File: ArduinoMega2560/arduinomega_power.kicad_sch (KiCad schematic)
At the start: 19 parts, among them IC5 LM358D, T2 FDN340P, U3 LP2986AILD-3.3/NOPB

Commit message: Annotation problem
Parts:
- renumbered RN5C1 to RN5C, IC5 to U3, U3 to UP3
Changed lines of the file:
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@@
   (symbol (lib_id "PCM_Amplifier_Operational_AKL:LM358D") (at 101.6 104.14 0) (unit 1)
     (in_bom yes) (on_board yes) (dnp no)
-    (property "Reference" "IC5" (at 113.03 99.9491 0)
+    (property "Reference" "U3" (at 113.03 99.9491 0)
       (effects (font (size 1.27 1.27)))
     )
@@
       (project "ArduinoMega2560"
         (path "/9c604cc5-1a6f-41a9-b015-ecf51c009c14/7c89fbb2-6a37-4d58-a5e8-241333b4d617"
-          (reference "IC5") (unit 1)
+          (reference "U3") (unit 1)
         )
       )
@@
   (symbol (lib_id "PCM_Amplifier_Operational_AKL:LM358D") (at 57.15 127 0) (unit 2)
     (in_bom yes) (on_board yes) (dnp no)
-    (property "Reference" "IC5" (at 58.42 116.84 0)
+    (property "Reference" "U3" (at 58.42 116.84 0)
       (effects (font (size 1.27 1.27)))
     )
@@
       (project "ArduinoMega2560"
         (path "/9c604cc5-1a6f-41a9-b015-ecf51c009c14/7c89fbb2-6a37-4d58-a5e8-241333b4d617"
-          (reference "IC5") (unit 2)
+          (reference "U3") (unit 2)
         )
       )
@@
   (symbol (lib_id "TI_LP2986AILD-3.3-NOPB:LP2986AILD-3.3_NOPB") (at 97.79 144.78 0) (unit 1)
     (in_bom yes) (on_board yes) (dnp no) (fields_autoplaced)
-    (property "Reference" "U3" (at 120.65 134.62 0)
+    (property "Reference" "UP3" (at 120.65 134.62 0)
       (effects (font (size 1.524 1.524)))
     )
@@
       (project "ArduinoMega2560"
         (path "/9c604cc5-1a6f-41a9-b015-ecf51c009c14/7c89fbb2-6a37-4d58-a5e8-241333b4d617"
-          (reference "U3") (unit 1)
+          (reference "UP3") (unit 1)
         )
       )
@@
       (effects (font (size 1.27 1.27)) hide)
     )
-    (property "Value" "GND1" (at 152.4 166.37 0)
-      (effects (font (size 1.27 1.27)))
+    (property "Value" "GND1" (at 154.94 162.56 0)
+      (effects (font (size 1.27 1.27)) (justify left))
     )
     (property "Footprint" "" (at 152.4 161.29 0)
@@
   (symbol (lib_id "PCM_Resistor_AKL:R_0603") (at 26.67 128.27 180) (unit 1)
     (in_bom yes) (on_board yes) (dnp no)
-    (property "Reference" "RN5C1" (at 29.21 127 0)
+    (property "Reference" "RN5C" (at 29.21 127 0)
       (effects (font (size 1.27 1.27)) (justify right))
     )
@@
       (project "ArduinoMega2560"
         (path "/9c604cc5-1a6f-41a9-b015-ecf51c009c14/7c89fbb2-6a37-4d58-a5e8-241333b4d617"
-          (reference "RN5C1") (unit 1)
-        )
-      )
+          (reference "RN5C") (unit 1)
+        )
+      )

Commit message: Daily update
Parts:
- renumbered RN5C to RN5C1

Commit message: Update label
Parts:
- renumbered LED_L1 to LED_PB7, LED_ON1 to ON1, RN3C1 to RN33, RN3D1 to RN34, RN5B1 to RN52, RN5C1 to RN53
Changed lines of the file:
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@@
 		(on_board yes)
 		(dnp no)
-		(property "Reference" "LED_ON1"
+		(property "Reference" "ON1"
 			(at 147.0025 95.25 0)
 			(effects
@@
 			(project "ArduinoMega2560"
 				(path "/9c604cc5-1a6f-41a9-b015-ecf51c009c14/7c89fbb2-6a37-4d58-a5e8-241333b4d617"
-					(reference "LED_ON1")
+					(reference "ON1")
 					(unit 1)
 				)
@@
 		(on_board yes)
 		(dnp no)
-		(property "Reference" "RN3C1"
+		(property "Reference" "RN33"
 			(at 158.75 96.52 90)
 			(effects
@@
 			(project "ArduinoMega2560"
 				(path "/9c604cc5-1a6f-41a9-b015-ecf51c009c14/7c89fbb2-6a37-4d58-a5e8-241333b4d617"
-					(reference "RN3C1")
+					(reference "RN33")
 					(unit 1)
 				)
@@
 		(on_board yes)
 		(dnp no)
-		(property "Reference" "RN5B1"
+		(property "Reference" "RN52"
 			(at 29.21 144.78 0)
 			(effects
@@
 			(project "ArduinoMega2560"
 				(path "/9c604cc5-1a6f-41a9-b015-ecf51c009c14/7c89fbb2-6a37-4d58-a5e8-241333b4d617"
-					(reference "RN5B1")
+					(reference "RN52")
 					(unit 1)
 				)
@@
 		(on_board yes)
 		(dnp no)
-		(property "Reference" "RN3D1"
+		(property "Reference" "RN34"
 			(at 158.75 109.22 90)
 			(effects
@@
 			(project "ArduinoMega2560"
 				(path "/9c604cc5-1a6f-41a9-b015-ecf51c009c14/7c89fbb2-6a37-4d58-a5e8-241333b4d617"
-					(reference "RN3D1")
+					(reference "RN34")
 					(unit 1)
 				)
@@
 		(on_board yes)
 		(dnp no)
-		(property "Reference" "RN5C1"
+		(property "Reference" "RN53"
 			(at 29.21 127 0)
 			(effects
@@
 			(project "ArduinoMega2560"
 				(path "/9c604cc5-1a6f-41a9-b015-ecf51c009c14/7c89fbb2-6a37-4d58-a5e8-241333b4d617"
-					(reference "RN5C1")
+					(reference "RN53")
 					(unit 1)
 				)
@@
 		(dnp no)
 		(fields_autoplaced yes)
-		(property "Reference" "LED_L1"
+		(property "Reference" "LED_PB7"
 			(at 147.0025 107.95 0)
 			(effects
@@
 			(project "ArduinoMega2560"
 				(path "/9c604cc5-1a6f-41a9-b015-ecf51c009c14/7c89fbb2-6a37-4d58-a5e8-241333b4d617"
-					(reference "LED_L1")
-					(unit 1)
-				)
+					(reference "LED_PB7")
+					(unit 1)
+				)

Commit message: Tracing
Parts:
- removed UP2: MC33269DTRK-5.0G, DPAK-3_ONS, symbol ON_Semi-MC33269DTRK-5.0G:MC33269DTRK-5.0G
- added U4: MC33269DTRK-5.0G, LDO_MC33269DTRK-5.0G_Onsemi:DPAK-3_ONS, symbol LDO_MC33269DTRK-5.0G_Onsemi:MC33269DTRK-5.0G
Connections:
- net GND1 is gone; now on net GND: C13.2
- net GNDPWR is gone; now on net GND: C2.2, Cp1.2, Jack1.2, Jack1.3
- net +5V: now also U4.2 (VOUT)
- net GND: now also U4.1 (GND/ADJ)
- net VCC renamed VIN
- net VIN: now also U4.3 (VIN)

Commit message: Update Trace
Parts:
- UP2: renamed from U4; footprint LDO_MC33269DTRK-5.0G_Onsemi:DPAK-3_ONS -> LDO_MC33269DTRK_5_0G_Onsemi:DPAK-3_ONS
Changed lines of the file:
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@@
 		(dnp no)
 		(fields_autoplaced yes)
-		(property "Reference" "U4"
+		(property "Reference" "UP2"
 			(at 99.06 62.23 0)
 			(effects
@@
 			)
 		)
-		(property "Footprint" "LDO_MC33269DTRK-5.0G_Onsemi:DPAK-3_ONS"
+		(property "Footprint" "LDO_MC33269DTRK_5_0G_Onsemi:DPAK-3_ONS"
 			(at 89.916 83.566 0)
 			(effects
@@
 			(project ""
 				(path "/9c604cc5-1a6f-41a9-b015-ecf51c009c14/7c89fbb2-6a37-4d58-a5e8-241333b4d617"
-					(reference "U4")
+					(reference "UP2")
 					(unit 1)
 				)

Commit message: Update
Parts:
- added J3, J4: PINHD_1x2_Male, Connector_PinHeader_2.54mm:PinHeader_1x02_P2.54mm_Vertical, symbol PCM_SL_Pin_Headers:PINHD_1x2_Male
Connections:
- net +5V: now also J3.1, J3.2
- net GND: now also J4.1, J4.2

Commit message: Update
Using Rev3
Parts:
- removed C11: 100nF_0603_16V, PCM_4ms_Capacitor:C_0603, symbol PCM_4ms_Capacitor:100nF_0603_16V
- removed J3, J4: PINHD_1x2_Male, Connector_PinHeader_2.54mm:PinHeader_1x02_P2.54mm_Vertical, symbol PCM_SL_Pin_Headers:PINHD_1x2_Male
- removed T2: FDN340P, PCM_Package_TO_SOT_SMD_AKL:SuperSOT-3, symbol PCM_Transistor_MOSFET_AKL:FDN340P
- removed U3: LM358D, PCM_Package_SO_AKL:SO-8_3.9x4.9mm_P1.27mm, symbol PCM_Amplifier_Operational_AKL:LM358D
- removed UP1: MC33269ST-5T3G, ON_Semi-MC33269ST-3.3T3G:ON_Semi-CASE_318E04_ISSUE_N-0-0-0, symbol ON_Semi-MC33269ST-3.3T3G:MC33269ST-3.3T3G
- removed UP2: MC33269DTRK-5.0G, LDO_MC33269DTRK_5_0G_Onsemi:DPAK-3_ONS, symbol LDO_MC33269DTRK-5.0G_Onsemi:MC33269DTRK-5.0G
- removed UP3: LP2986AILD-3.3/NOPB, TI_LP2986AILD-3.3-NOPB:LDC08A, symbol TI_LP2986AILD-3.3-NOPB:LP2986AILD-3.3_NOPB
- added PS1: LD1117S50CTR, LDO_LD1117S50CTR_STMicroelectronics:SOT-223_STM, symbol LDO_LD1117S50CTR_STMicroelectronics:LD1117S50CTR
- added PS2: LP2985-3.3, Package_TO_SOT_SMD:SOT-23-5, symbol Regulator_Linear:LP2985-3.3
- added T1: PMV48XP_215, TO-236_SOT23_NEX, symbol MOSFET_PMV48XP,215_Nexperia:PMV48XP_215
- added U3: LMV358IDGK, PCM_Package_SO_AKL:MSOP-8_3x3mm_P0.65mm, symbol PCM_Amplifier_Operational_AKL:LMV358IDGK
- C13: Display 0.1uF -> 1uF
- renumbered RN33 to RN31, RN34 to RN32, RN52 to RN54
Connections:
- net +3.3V: now also PS2.5 (VOUT), U3.6 (-)
- net +5V: now also PS1.2 (VOUT), PS2.1 (VIN), PS2.3 (ON/~{OFF}), T1.2 (S), U3.8 (V+)
- net GATE_CMD: now also T1.1 (G), U3.7
- net GND: now also PS1.1 (ADJ/GND), PS2.2 (GND), U3.4 (V-)
- net PB7: now also U3.3 (+); no longer RN32.2
- net USBVCC: now also T1.3 (D)
- net VIN: now also PS1.3 (VIN)
- net CMP: now reaches C12.1, RN53.1, RN54.2
- net CMP: now also U3.5 (+)
- new net: RN32.2, U3.1, U3.2 (-)
- no-connect marks 6 -> 1
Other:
- moved on the sheet: C13, Cp2, LED_PB7, ON1, RN31, RN32

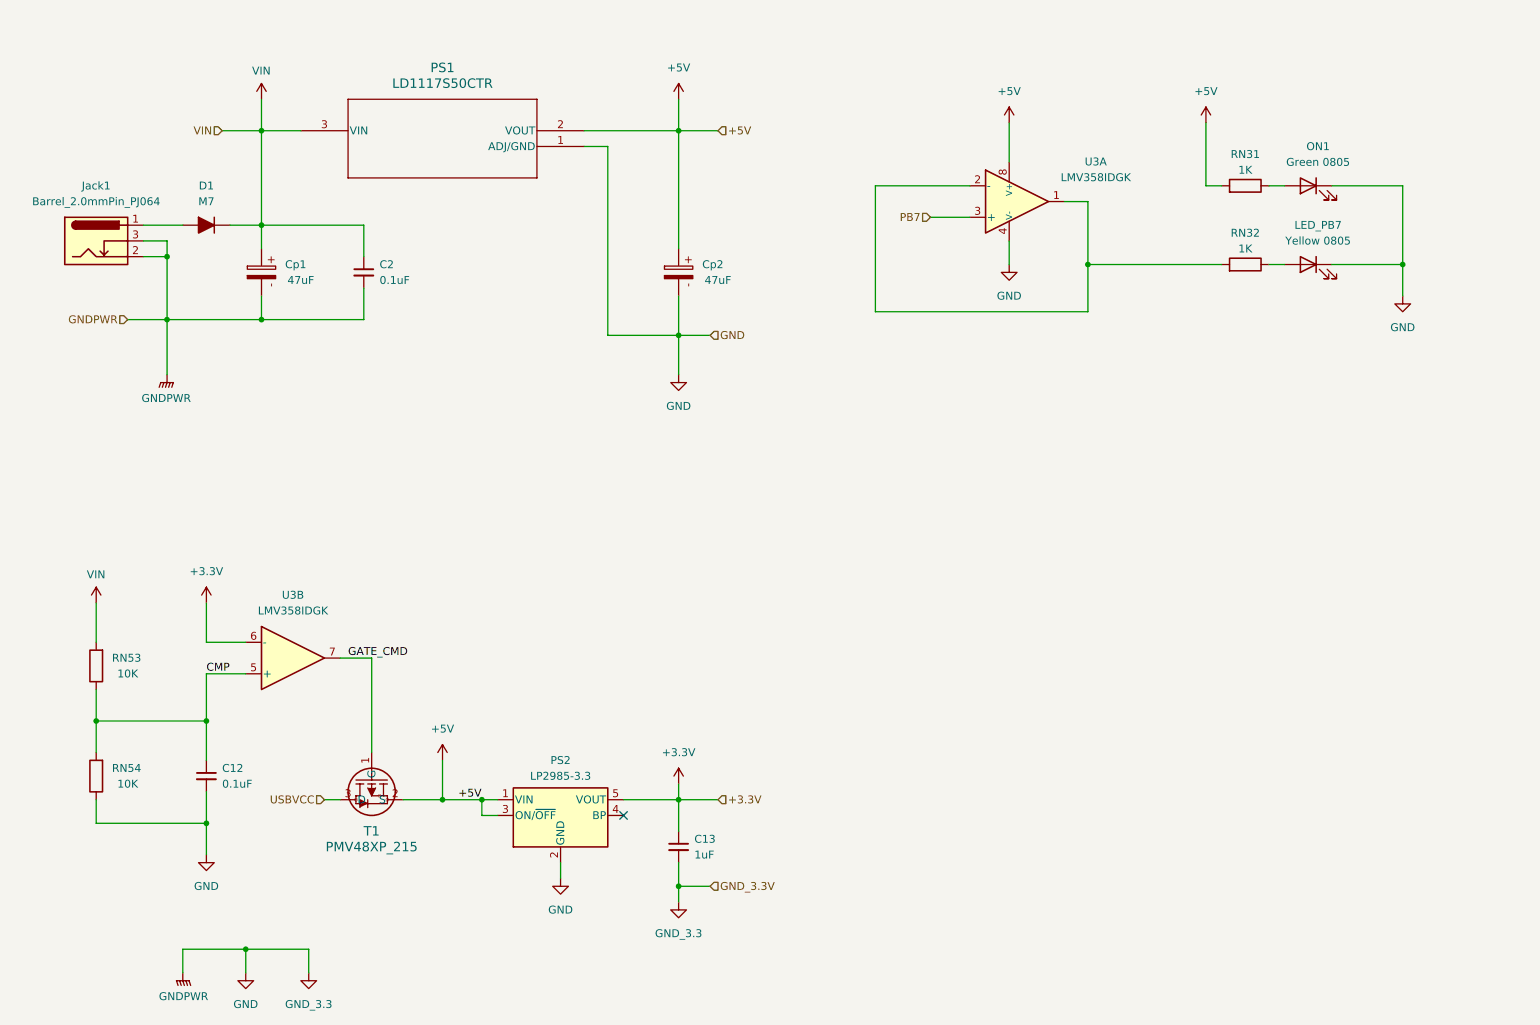
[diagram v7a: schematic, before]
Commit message: Delete old components
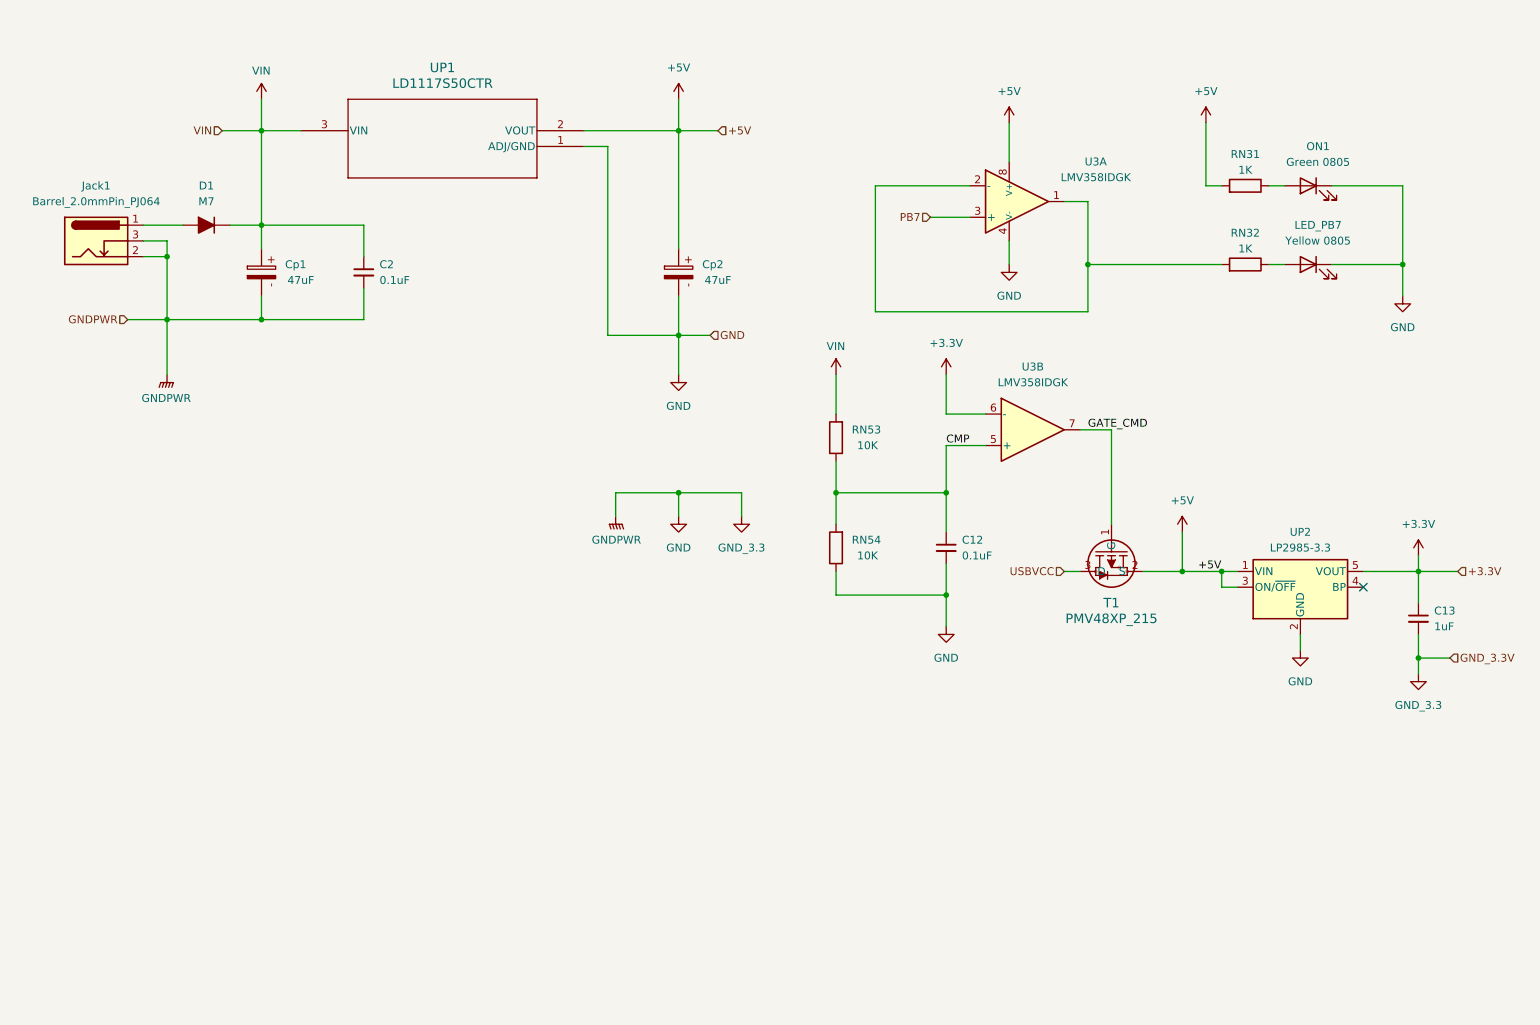
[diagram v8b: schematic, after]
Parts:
- renumbered PS1 to UP1, PS2 to UP2
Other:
- moved on the sheet: C12, C13, RN53, RN54, T1, U3B, UP2
